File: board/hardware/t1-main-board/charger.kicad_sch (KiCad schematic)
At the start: 0 parts

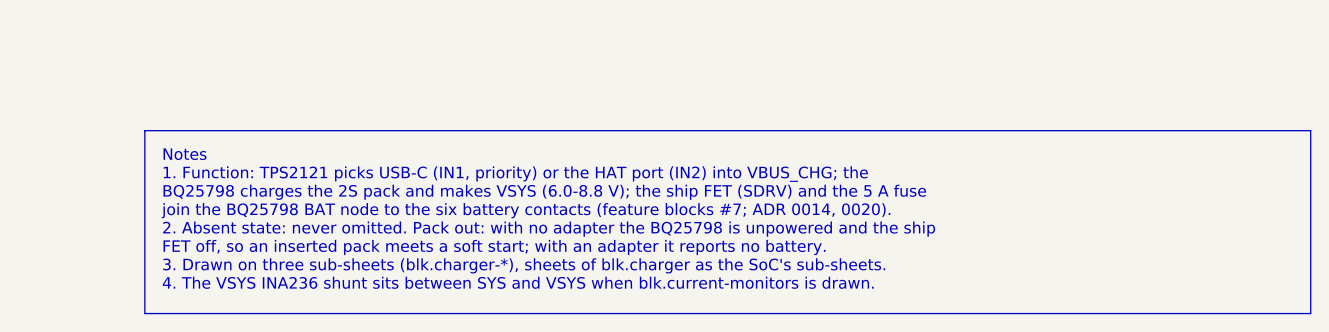
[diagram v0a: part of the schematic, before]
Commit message: Board: capture blk.current-monitors
Five INA236 on I2C1 (0x40-0x43, 0x48) with their shunts, per power tree
§4.12 and BOM v1 lines 54 and 136. The measured branches are rails of
their own (VSYS_SRC, VSYS_LV_AUDIO, VSYS_AUDIO, VSYS_LV_BL, VSYS_P5V1),
fed through the shunts on this sheet; the charger, audio, backlight and
5.1 V sheets take them. The root's layout may leave a stack level empty,
so the block sits under the notes; IC bboxes hold turned rail values;
passive rows hold a bottom rail's text.

Co-Authored-By: Claude Opus 5.5 <noreply@anthropic.com>
Claude-Session: https://claude.ai/code/session_01Ei262h3TpgY9vyfNLMi5Mn
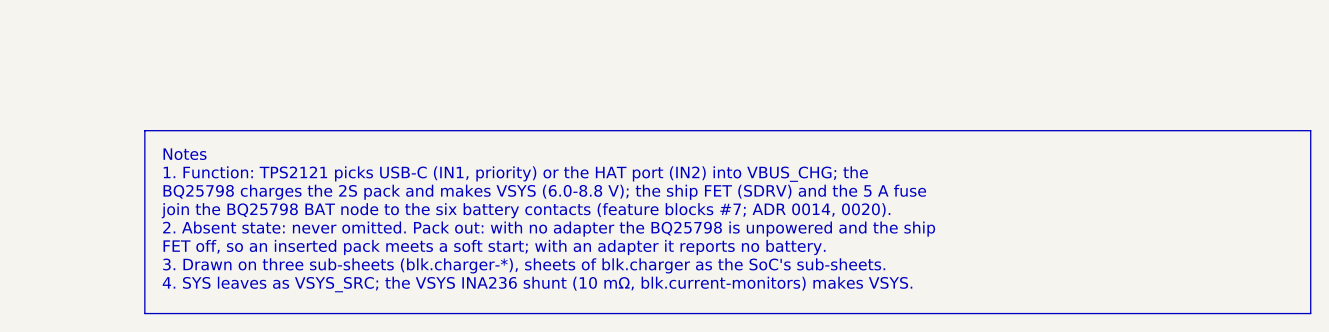
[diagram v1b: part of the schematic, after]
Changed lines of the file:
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@@
 (paper "A4")
 (title_block (title "Charger and battery path") (date "2026-10-25") (rev "A") (company "The OpenDAP Project") (comment 1 "blk.charger") (comment 2 "TPS2121 input mux, BQ25798 2S charger, ship FET, fuse and the six battery contacts"))
-(text_box "Notes\n1. Function: TPS2121 picks USB-C (IN1, priority) or the HAT port (IN2) into VBUS_CHG; the\n   BQ25798 charges the 2S pack and makes VSYS (6.0-8.8 V); the ship FET (SDRV) and the 5 A fuse\n   join the BQ25798 BAT node to the six battery contacts (feature blocks #7; ADR 0014, 0020).\n2. Absent state: never omitted. Pack out: with no adapter the BQ25798 is unpowered and the ship\n   FET off, so an inserted pack meets a soft start; with an adapter it reports no battery.\n3. Drawn on three sub-sheets (blk.charger-*), sheets of blk.charger as the SoC's sub-sheets.\n4. The VSYS INA236 shunt sits between SYS and VSYS when blk.current-monitors is drawn." (exclude_from_sim no) (at 152.4 140.97 0) (size 129.54 20.32) (margins 1.905 1.905 1.905 1.905) (stroke (width 0) (type default)) (fill (type none)) (effects (font (size 1.27 1.27)) (justify left top)))
+(text_box "Notes\n1. Function: TPS2121 picks USB-C (IN1, priority) or the HAT port (IN2) into VBUS_CHG; the\n   BQ25798 charges the 2S pack and makes VSYS (6.0-8.8 V); the ship FET (SDRV) and the 5 A fuse\n   join the BQ25798 BAT node to the six battery contacts (feature blocks #7; ADR 0014, 0020).\n2. Absent state: never omitted. Pack out: with no adapter the BQ25798 is unpowered and the ship\n   FET off, so an inserted pack meets a soft start; with an adapter it reports no battery.\n3. Drawn on three sub-sheets (blk.charger-*), sheets of blk.charger as the SoC's sub-sheets.\n4. SYS leaves as VSYS_SRC; the VSYS INA236 shunt (10 mΩ, blk.current-monitors) makes VSYS." (exclude_from_sim no) (at 152.4 140.97 0) (size 129.54 20.32) (margins 1.905 1.905 1.905 1.905) (stroke (width 0) (type default)) (fill (type none)) (effects (font (size 1.27 1.27)) (justify left top)))
 (sheet (at 38.1 30.48) (size 50.8 12.7) (exclude_from_sim no) (in_bom yes) (on_board yes) (dnp no) (fields_autoplaced yes) (stroke (width 0.1524) (type solid)) (fill (color 0 0 0 0.0000))
   (property "Sheetname" "Charger: input mux" (at 38.1 29.7684 0) (effects (font (size 1.27 1.27)) (justify left bottom)))
